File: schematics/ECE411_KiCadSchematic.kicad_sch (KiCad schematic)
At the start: 5 parts, among them SW1 Main Button

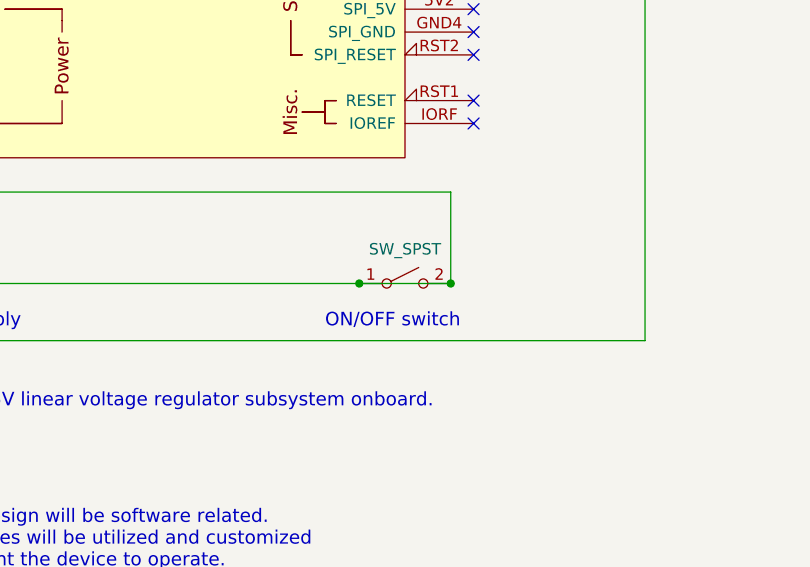
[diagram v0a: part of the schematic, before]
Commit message: update extra line across power switch
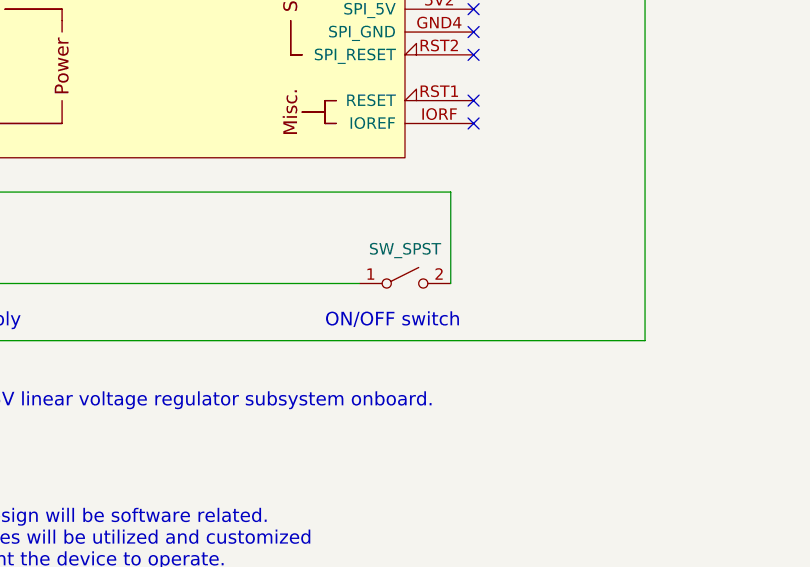
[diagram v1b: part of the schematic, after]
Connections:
- net at KCD1-1-101-ON-OFF-X1.2 (B), XA1.VIN: no longer BT1.1 (+), KCD1-1-101-ON-OFF-X1.1 (A)
- new net: BT1.1 (+), KCD1-1-101-ON-OFF-X1.1 (A)
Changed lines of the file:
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@@
   (junction (at 46.99 102.87) (diameter 0) (color 0 0 0 0)
   )
-  (junction (at 125.73 102.87) (diameter 0) (color 0 0 0 0)
-  )
   (junction (at 46.99 72.39) (diameter 0) (color 0 0 0 0)
-  )
-  (junction (at 115.57 102.87) (diameter 0) (color 0 0 0 0)
   )
   (no_connect (at 62.23 74.93))
@@
     (stroke (width 0) (type default) (color 0 0 0 0))
   )
-  (wire (pts (xy 115.57 102.87) (xy 125.73 102.87))
-    (stroke (width 0) (type default) (color 0 0 0 0))
-  )

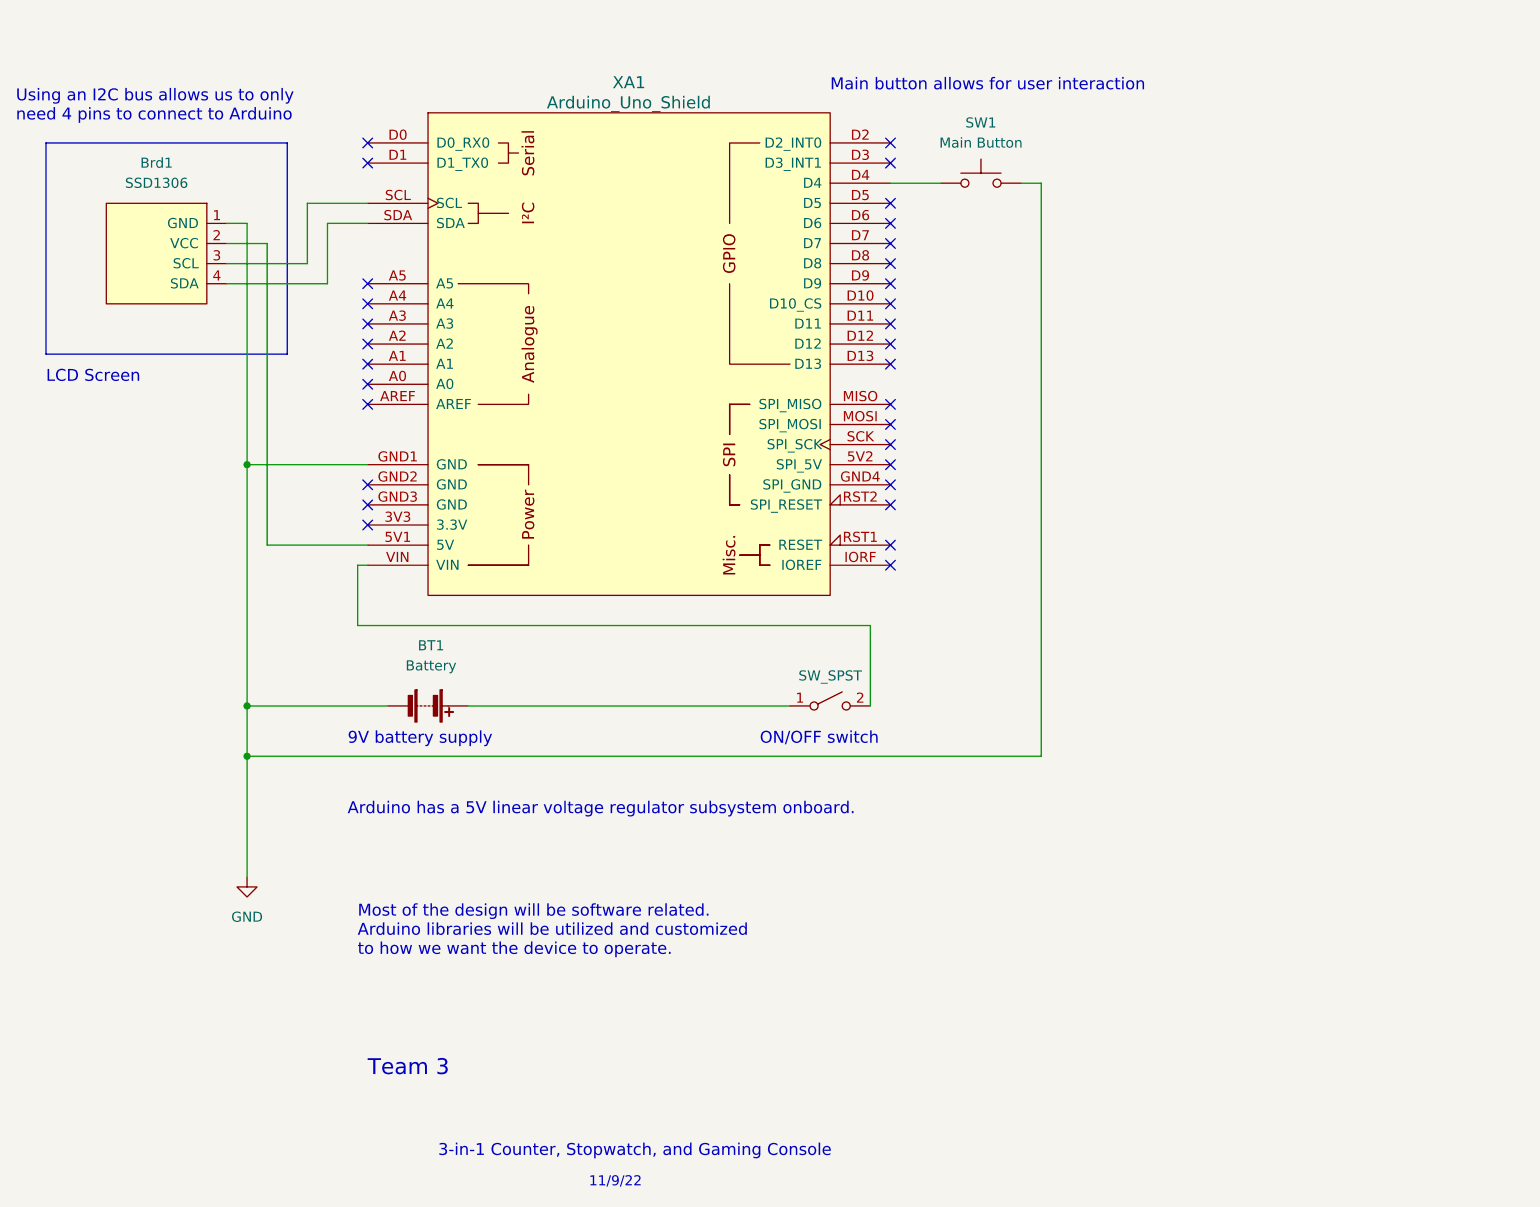
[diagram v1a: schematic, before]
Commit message: updated pcb and circuit schematic
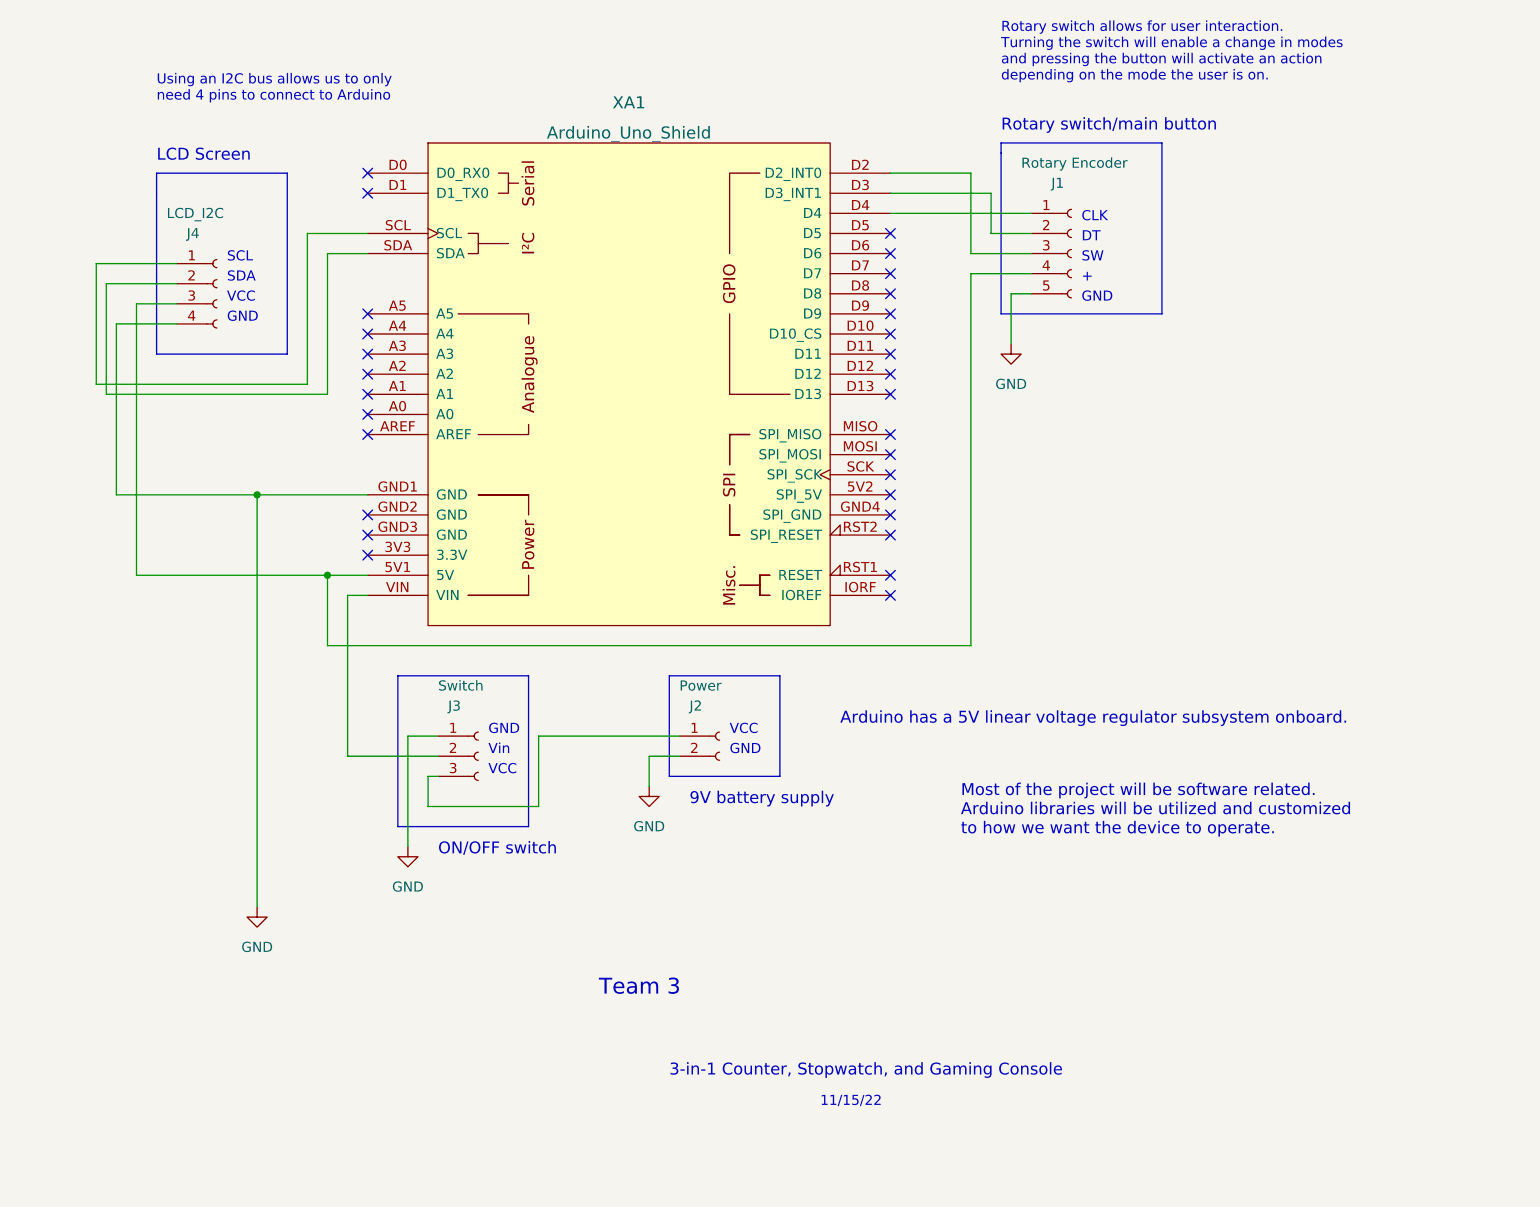
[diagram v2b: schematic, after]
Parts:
- removed BT1: Battery, symbol Device:Battery
- removed Brd1: SSD1306, footprints:SSD1306-128x64_OLED, symbol SSD1306-128x64_OLED:SSD1306
- removed KCD1-1-101-ON-OFF-X1: SW_SPST, symbol Switch:SW_SPST
- removed SW1: Main Button, symbol Switch:SW_Push
- added J1: Rotary Encoder, Connector_PinSocket_2.54mm:PinSocket_1x05_P2.54mm_Horizontal, symbol Connector:Conn_01x05_Female
- added J2: Power, Connector_PinSocket_2.54mm:PinSocket_1x02_P2.54mm_Horizontal, symbol Connector:Conn_01x02_Female
- added J3: Switch, Connector_PinSocket_2.54mm:PinSocket_1x03_P2.54mm_Vertical, symbol Connector:Conn_01x03_Female
- added J4: LCD_I2C, Connector_PinSocket_2.54mm:PinSocket_1x04_P2.54mm_Horizontal, symbol Connector:Conn_01x04_Female
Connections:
- net GND: now also J1.5 (Pin_5), J2.2 (Pin_2), J3.1 (Pin_1), J4.4 (Pin_4)
- net at XA1.5V1 (5V): now also J1.4 (Pin_4), J4.3 (Pin_3)
- net at XA1.D2 (D2_INT0): now also J1.3 (Pin_3)
- net at XA1.D3 (D3_INT1): now also J1.2 (Pin_2)
- net at XA1.D4: now also J1.1 (Pin_1)
- net at XA1.SCL: now also J4.1 (Pin_1)
- net at XA1.SDA: now also J4.2 (Pin_2)
- net at XA1.VIN: now also J3.2 (Pin_2)
- new net: J2.1 (Pin_1), J3.3 (Pin_3)
- no-connect marks 31 -> 29
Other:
- note added: "+"
- note added: "11/15/22"
- note added: "CLK"
- note added: "DT"
- note added: "GND"
- note added: "Most of the project will be software related. Arduino libraries will be utilized and customized to how we want the device to operate."
- note added: "Rotary switch allows for user interaction. Turning the switch will enable a change in modes and pressing the button will activate an action depending on the mode the user is on."
- note added: "Rotary switch/main button"
- note added: "SCL"
- note added: "SDA"
- note added: "SW"
- note added: "VCC"
- note added: "Vin"
- note removed: "11/9/22"
- note removed: "Main button allows for user interaction"
- note removed: "Most of the design will be software related. Arduino libraries will be utilized and customized to how we want the device to operate."
- moved on the sheet: XA1
